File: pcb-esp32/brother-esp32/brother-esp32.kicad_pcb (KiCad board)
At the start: 2 copper layers, 85.2 x 50.3 mm, 77 parts, among them J1 Conn_01x40_Female, U1 SST39SF040-55-4I-WHE, U2 ESP32-DEVKITC_WROOM, U3 MCP23016-I/SO

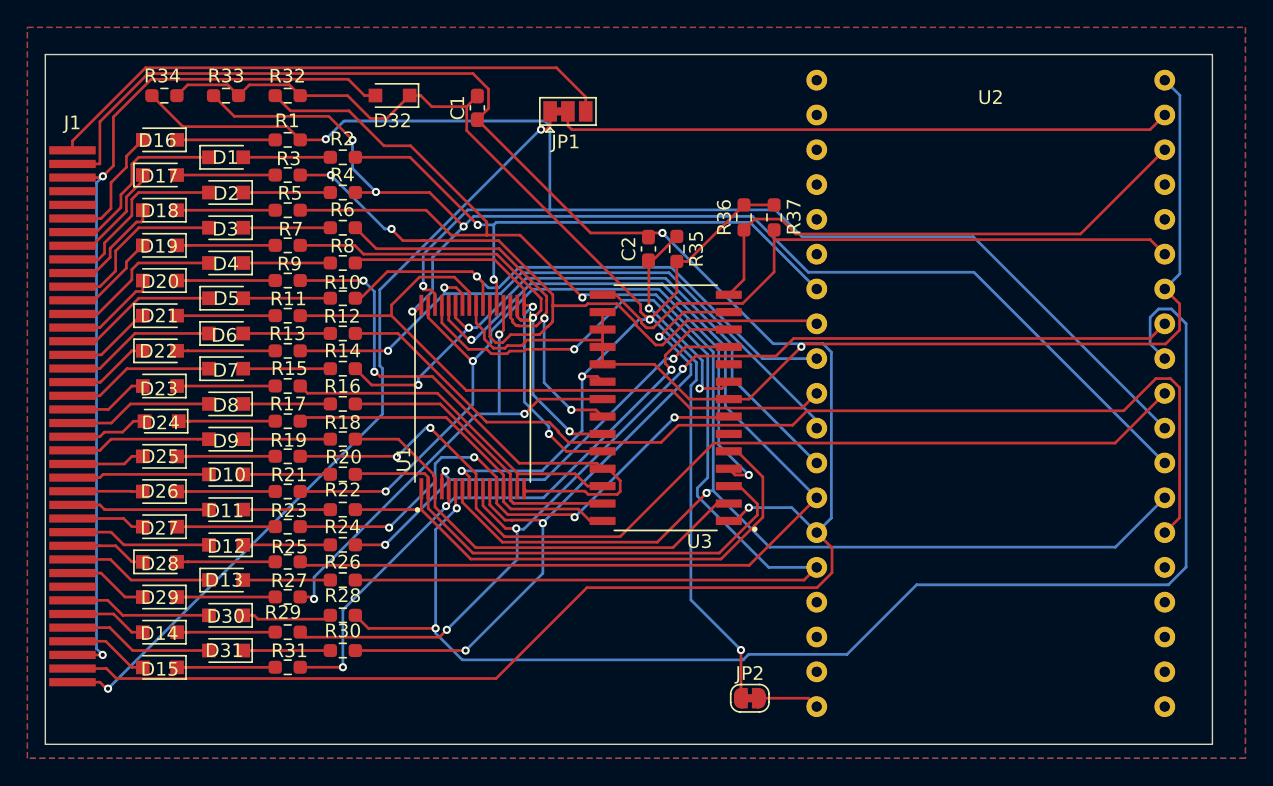
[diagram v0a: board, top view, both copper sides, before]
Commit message: Updated design remove diodes
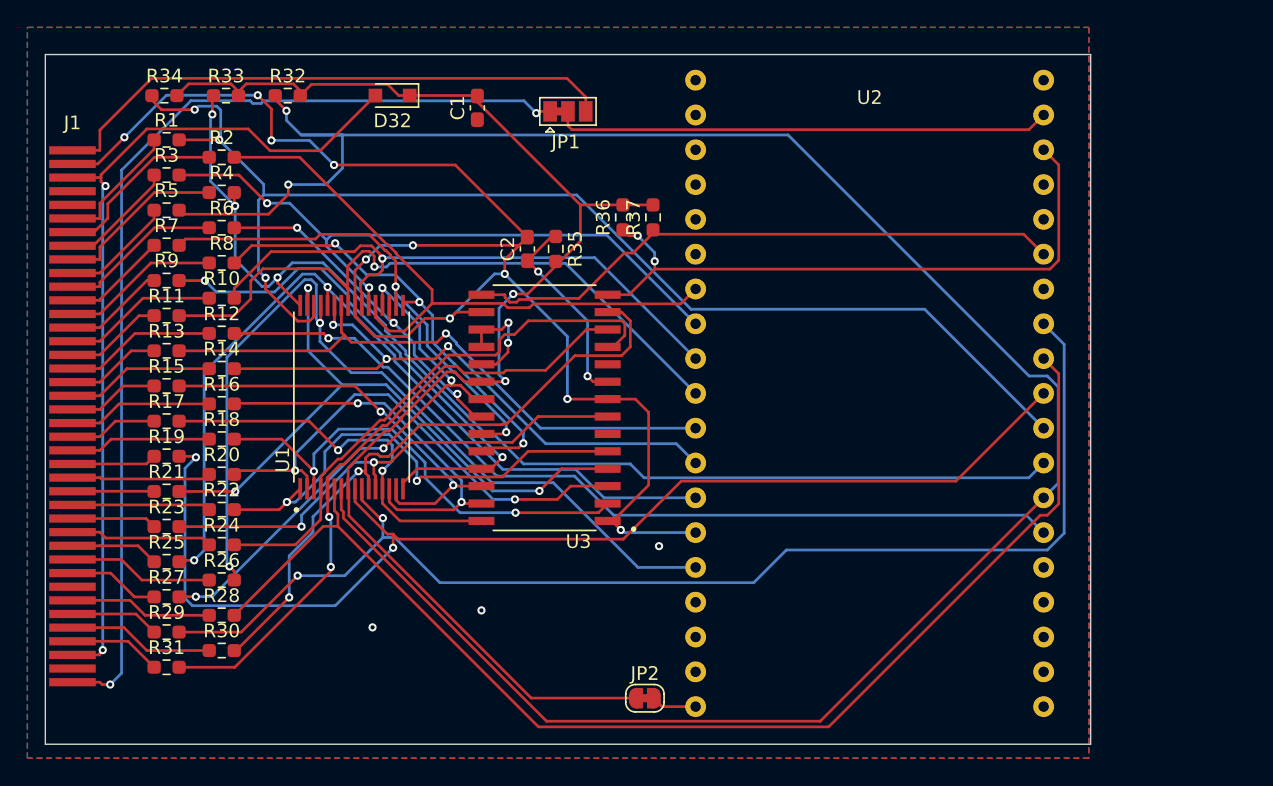
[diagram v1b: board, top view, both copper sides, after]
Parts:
- removed D1, D10, D11, D12, D13, D14, D15, D16, D17, D18, D19, D2, D20, D21, D22, D23, D24, D25, D26, D27, D28, D29, D3, D30, D31, D4, D5, D6, D7, D8, D9: D, Diode_SMD:D_SOD-323_HandSoldering
- R1, R10, R11, R12, R13, R14, R15, R16, R17, R18, R19, R2, R20, R21, R22, R23, R24, R25, R26, R27, R28, R29, R3, R30, R31, R32, R33, R34, R35, R36, R37, R4, R5, R6, R7, R8, R9: footprint Resistor_SMD:R_0603_1608Metric_Pad0.98x0.95mm_HandSolder -> Resistor:R_0603_1608Metric_Pad0.98x0.95mm_HandSolder
- moved C2 8.84 mm to (100.0, 49.2)
- moved R1 8.84 mm to (73.7, 41.2)
- moved R11 8.84 mm to (73.7, 54.1)
- moved R13 8.84 mm to (73.7, 56.6)
- moved R15 8.84 mm to (73.7, 59.2)
- moved R17 8.84 mm to (73.7, 61.8)
- moved R19 8.84 mm to (73.7, 64.3)
- moved R21 8.84 mm to (73.7, 66.9)
- moved R23 8.84 mm to (73.7, 69.5)
- moved R25 8.84 mm to (73.7, 72.0)
- moved R27 8.84 mm to (73.7, 74.6)
- moved R29 8.84 mm to (73.7, 77.2)
- moved R3 8.84 mm to (73.7, 43.8)
- moved R31 8.84 mm to (73.7, 79.7)
- moved R35 8.84 mm to (102.1, 49.2)
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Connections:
- J1 pad 10: Net-(D18-Pad2) -> Net-(J1-Pad10)
- J1 pad 11: Net-(D3-Pad2) -> Net-(J1-Pad11)
- J1 pad 12: Net-(D19-Pad2) -> Net-(J1-Pad12)
- J1 pad 13: Net-(D4-Pad2) -> Net-(J1-Pad13)
- J1 pad 14: Net-(D20-Pad2) -> Net-(J1-Pad14)
- J1 pad 15: Net-(D5-Pad1) -> Net-(J1-Pad15)
- J1 pad 16: Net-(D21-Pad1) -> Net-(J1-Pad16)
- J1 pad 17: Net-(D6-Pad1) -> Net-(J1-Pad17)
- J1 pad 18: Net-(D22-Pad1) -> Net-(J1-Pad18)
- J1 pad 19: Net-(D7-Pad1) -> Net-(J1-Pad19)
- J1 pad 20: Net-(D23-Pad2) -> Net-(J1-Pad20)
- J1 pad 21: Net-(D8-Pad2) -> Net-(J1-Pad21)
- J1 pad 22: Net-(D24-Pad2) -> Net-(J1-Pad22)
- J1 pad 23: Net-(D9-Pad2) -> Net-(J1-Pad23)
- J1 pad 24: Net-(D25-Pad2) -> Net-(J1-Pad24)
- J1 pad 25: Net-(D10-Pad2) -> Net-(J1-Pad25)
- J1 pad 26: Net-(D26-Pad2) -> Net-(J1-Pad26)
- J1 pad 27: Net-(D11-Pad2) -> Net-(J1-Pad27)
- J1 pad 28: Net-(D27-Pad2) -> Net-(J1-Pad28)
- J1 pad 29: Net-(D12-Pad2) -> Net-(J1-Pad29)
- J1 pad 30: Net-(D28-Pad1) -> Net-(J1-Pad30)
- J1 pad 31: Net-(D13-Pad1) -> Net-(J1-Pad31)
- J1 pad 32: Net-(D29-Pad2) -> Net-(J1-Pad32)
- J1 pad 34: Net-(D30-Pad2) -> Net-(J1-Pad34)
- J1 pad 35: Net-(D14-Pad2) -> Net-(J1-Pad35)
- J1 pad 36: Net-(D31-Pad2) -> Net-(J1-Pad36)
- J1 pad 37: Net-(D15-Pad2) -> Net-(J1-Pad37)
- J1 pad 6: Net-(D16-Pad2) -> Net-(J1-Pad6)
- J1 pad 7: Net-(D1-Pad1) -> Net-(J1-Pad7)
- J1 pad 8: Net-(D17-Pad1) -> Net-(J1-Pad8)
- J1 pad 9: Net-(D2-Pad2) -> Net-(J1-Pad9)
- R1 pad 1: Net-(D16-Pad1) -> Net-(J1-Pad6)
- R10 pad 1: Net-(D5-Pad2) -> Net-(J1-Pad15)
- R11 pad 1: Net-(D21-Pad2) -> Net-(J1-Pad16)
- R12 pad 1: Net-(D6-Pad2) -> Net-(J1-Pad17)
- R13 pad 1: Net-(D22-Pad2) -> Net-(J1-Pad18)
- R14 pad 1: Net-(D7-Pad2) -> Net-(J1-Pad19)
- R15 pad 1: Net-(D23-Pad1) -> Net-(J1-Pad20)
- R16 pad 1: Net-(D8-Pad1) -> Net-(J1-Pad21)
- R17 pad 1: Net-(D24-Pad1) -> Net-(J1-Pad22)
- R18 pad 1: Net-(D9-Pad1) -> Net-(J1-Pad23)
- R19 pad 1: Net-(D25-Pad1) -> Net-(J1-Pad24)
- R2 pad 1: Net-(D1-Pad2) -> Net-(J1-Pad7)
- R20 pad 1: Net-(D10-Pad1) -> Net-(J1-Pad25)
- R21 pad 1: Net-(D26-Pad1) -> Net-(J1-Pad26)
- R22 pad 1: Net-(D11-Pad1) -> Net-(J1-Pad27)
- R23 pad 1: Net-(D27-Pad1) -> Net-(J1-Pad28)
- R24 pad 1: Net-(D12-Pad1) -> Net-(J1-Pad29)
- R25 pad 1: Net-(D28-Pad2) -> Net-(J1-Pad30)
- R26 pad 1: Net-(D13-Pad2) -> Net-(J1-Pad31)
- R27 pad 1: Net-(D29-Pad1) -> Net-(J1-Pad32)
- R28 pad 1: Net-(D30-Pad1) -> Net-(J1-Pad34)
- R29 pad 1: Net-(D14-Pad1) -> Net-(J1-Pad35)
- R3 pad 1: Net-(D17-Pad2) -> Net-(J1-Pad8)
- R30 pad 1: Net-(D31-Pad1) -> Net-(J1-Pad36)
- R31 pad 1: Net-(D15-Pad1) -> Net-(J1-Pad37)
- R4 pad 1: Net-(D2-Pad1) -> Net-(J1-Pad9)
- R5 pad 1: Net-(D18-Pad1) -> Net-(J1-Pad10)
- R6 pad 1: Net-(D3-Pad1) -> Net-(J1-Pad11)
- R7 pad 1: Net-(D19-Pad1) -> Net-(J1-Pad12)
- R8 pad 1: Net-(D4-Pad1) -> Net-(J1-Pad13)
- R9 pad 1: Net-(D20-Pad1) -> Net-(J1-Pad14)
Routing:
- net GND: track 235.5 -> 118.2 mm, vias 3 -> 15
- net WE: track 123.1 -> 160.6 mm
- net Q6: track 79.1 -> 62.4 mm, vias 1 -> 2
- net PRE_BOT: track 58.7 -> 74.7 mm
- net Q7: track 80.4 -> 65.3 mm, vias 1 -> 2
- net A18: track 73.0 -> 86.8 mm
- net Net-(D1-Pad1): track 13.6 -> 0.00 mm
- net +5V: track 115.1 -> 101.6 mm, vias 4 -> 2
- net Net-(D2-Pad2): track 13.1 -> 0.00 mm
- net Net-(J1-Pad7): track 0.00 -> 12.9 mm
- net Net-(D3-Pad2): track 12.6 -> 0.00 mm
- net Net-(J1-Pad9): track 0.00 -> 12.5 mm
- net A16: track 78.5 -> 90.5 mm, vias 3 -> 2
- net Net-(J1-Pad11): track 0.00 -> 11.9 mm
- net Net-(D4-Pad2): track 11.9 -> 0.00 mm
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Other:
- board size 85.2 x 50.3 mm -> 76.3 x 50.3 mm
